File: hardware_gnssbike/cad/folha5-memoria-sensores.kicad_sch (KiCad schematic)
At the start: 18 parts, among them U501 MX25R6435F, U502 Bosch BMP585, U503 Bosch BMI270, U504 Memsic MMC5603NJ, U505 TI OPT3001DNPR

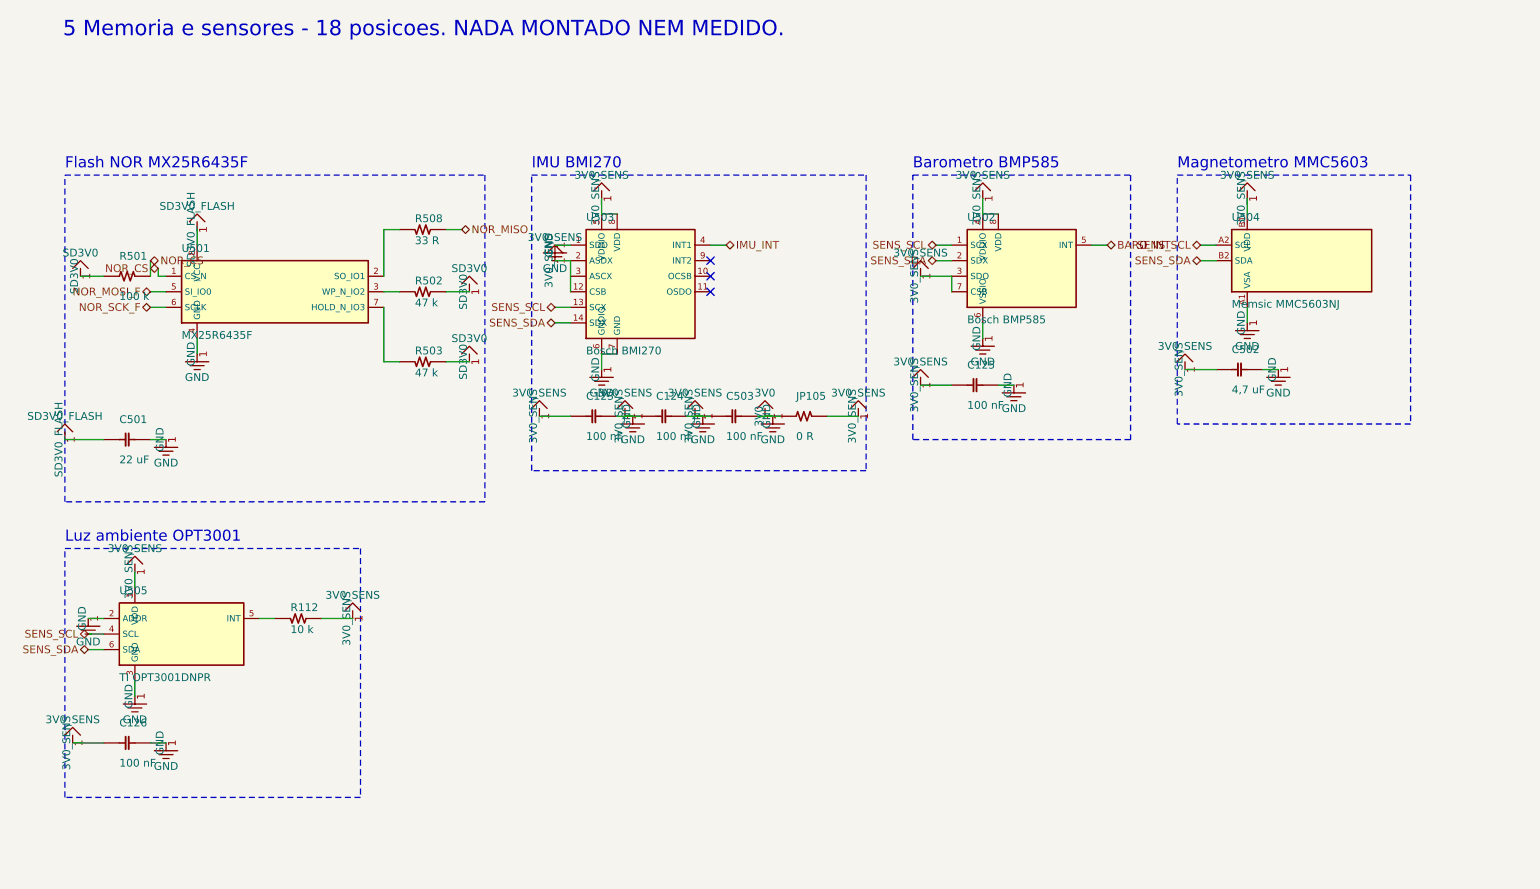
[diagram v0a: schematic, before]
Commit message: feat(hardware): spread the schematic so references, values and labels stay apart
The owner asked for the block-drawn schematic to be readable: designators
and labels were printing over each other. Power symbols now hide the pin
number and name (each printed a "1" and the rail's name twice) and point
away from their pin, lying along the line of a side pin with the name on
that line; the decoupling shelf is a row of stood-up capacitors per rail
with one wire along the tops and one symbol per row, test points standing
too; references and values sit to the right of a standing part and between
the neighbouring lines of a lying one, and block titles, part texts and
symbol names are obstacles for the router and for symbol and label
placement. Pull-ups and pull-downs of a labelled line stand past the label,
and off the corridor when the line goes on to another anchor; the labels'
room is reserved before the members are placed; the FPC connector is
mirrored to face the panel and aligned with it, its board-side wire
continuing from the label point, with the two nets of a pass-through pin
allowed to share cells; the two cells in front of every pin belong to its
net; DISP_VDD is drawn as a rail; blocks are packed by height and sheet 1
fits an A3.

The library symbol now always holds the base drawing and the instance
carries the rotation and mirror. The generator used to write the library
already flipped and the (mirror ...) token as well, applying the transform
twice, and the earlier "measurement" of (mirror x) was inverted by that.
Measured again on minimal files: (mirror y) swaps left for right, an
instance at 90 sends the left pin to the bottom, and KiCad transforms the
field justification along with the instance.

check_sch.py passes: the netlist equals nets.py pin by pin, no new ERC
error, no wire over a component. Eight nets are closed by labels where the
maze found no path inside the block, and the solar harvester and the left
of the gauge remain crowded; SCH_DEBUG=1 exp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
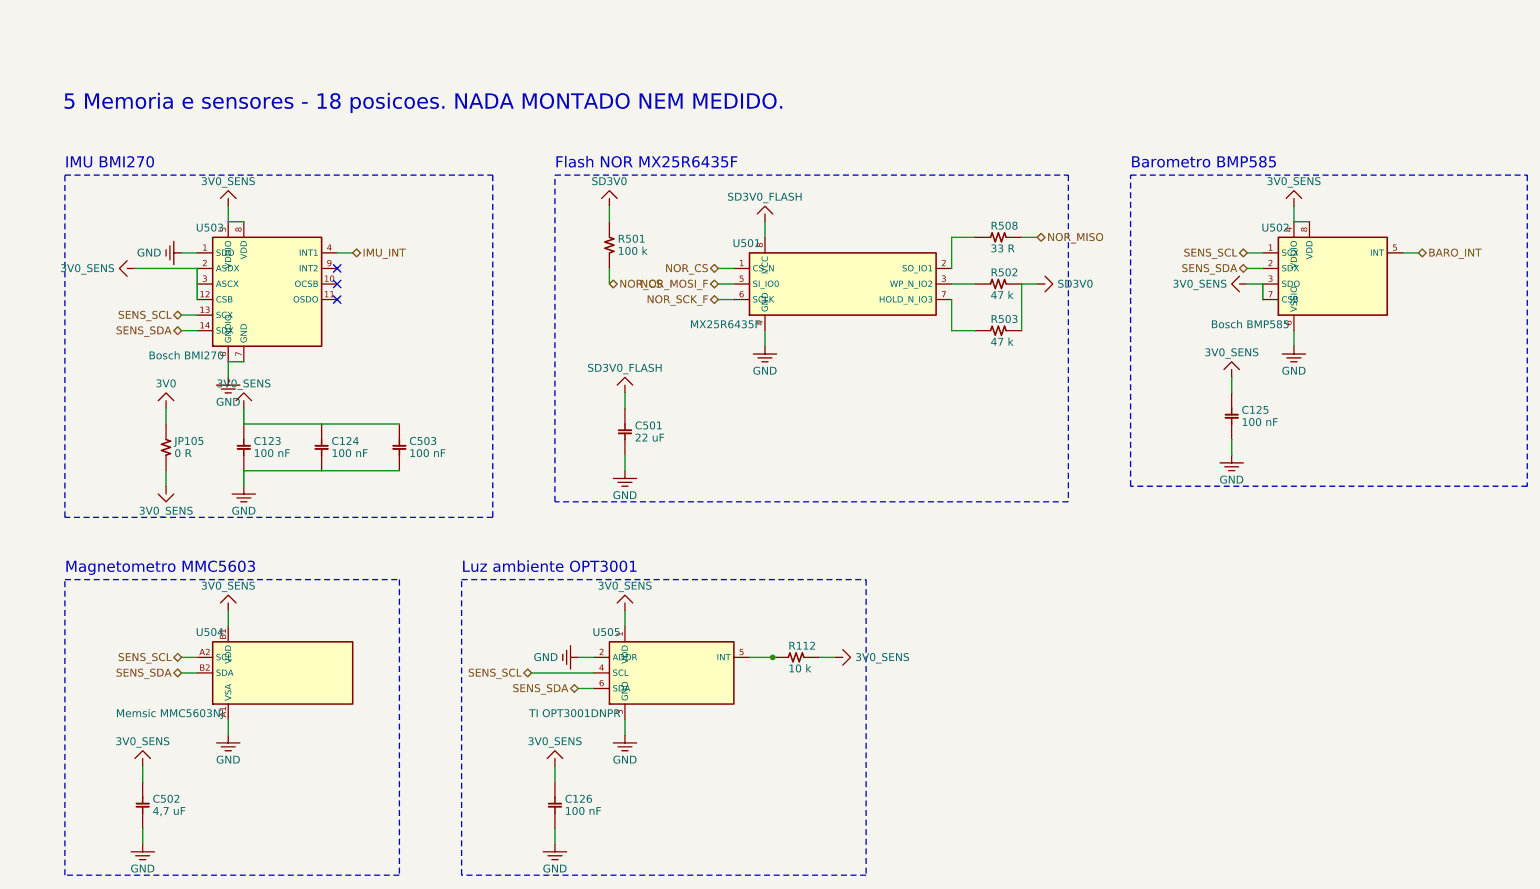
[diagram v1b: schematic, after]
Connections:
- net 3V0: no longer C123.1, C123.2, C124.1, C124.2, C125.1, C125.2, C126.1, C126.2, C501.2, C502.1, C502.2, C503.1, C503.2, JP105.2, R112.1, U501.4 (GND), U502.3 (SDO), U502.4 (VDDIO), U502.6 (VSSIO), U502.7 (CSB), U502.8 (VDD), U503.1 (SDO), U503.12 (CSB), U503.2 (ASDX), U503.3 (ASCX), U503.5 (VDDIO), U503.6 (GNDIO), U503.7 (GND), U503.8 (VDD), U504.A1 (VSA), U504.B1 (VDD), U505.1 (VDD), U505.2 (ADDR), U505.3 (GND)
- new net 3V0_SENS: C123.1, C124.1, C125.1, C126.1, C502.1, C503.1, JP105.2, R112.1, U502.3 (SDO), U502.4 (VDDIO), U502.7 (CSB), U502.8 (VDD), U503.12 (CSB), U503.2 (ASDX), U503.3 (ASCX), U503.5 (VDDIO), U503.8 (VDD), U504.B1 (VDD), U505.1 (VDD)
- new net GND: C123.2, C124.2, C125.2, C126.2, C501.2, C502.2, C503.2, U501.4 (GND), U502.6 (VSSIO), U503.1 (SDO), U503.6 (GNDIO), U503.7 (GND), U504.A1 (VSA), U505.2 (ADDR), U505.3 (GND)
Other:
- moved on the sheet: C123, C124, C125, C126, C501, C502, C503, JP105, R112, R501, R502, R503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

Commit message: feat(hardware): apply the schematic review, take either display, review the case
Apply the corrections the owner approved on 2026-10-18, in the
generators: the BMP585 land from figure 29, the RGB LED land unmirrored,
the TLV7031DCKR renumbered and fed from VBAT_SYS, the common pad of
JP301 in the middle, the OPT3001 exposed pad, the Murata land for the
buck inductors, 10 uF on PVDD and 3V3BL, a 24 V TVS on VBUS, the flash
on 3V0, pin-1 marks, the charge LEDs in the key row, the TVS next to
their connectors, the USB-C on the maker's edge line, the Same Sky
buzzer in place of the last-time-buy Murata, and an LCSC code on every
fitted part.

The board takes the JDI or the Sharp on one dual-contact Molex 503480:
JP401 picks 3V0 or 5V0, and a TPS610997 boost feeds the Sharp. A second
blind check found the connector drawn backwards (the tail enters on the
nail side); the land, the circuit order and the boost placement follow
the drawings now.

The router finds its way further: unique UUIDs per footprint, so the
DRC names the right pads; the chip antenna's own nets inside its
keep-out; JP301 turned so the two RF lines do not cross; ground vias
outside the dense chips, bent and geometrically checked ground stubs,
and a pass with the power rails first. The DRC reports no error; 60
items are still unconnected.

The case is reviewed part by part (hardware_gnssbike/12): the solar
module pockets follow the datasheet's +-0.3 mm (the case grows to 64 mm),
the keys stop 0.15 mm under the membrane, and the light sensor gets a
sealed window. The sealing of the USB-C, the floor holes and the lid
seam is left to the owner. The documents follow parts.py.

Nothing is fabricated, and the routing is still open.
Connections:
- net SD3V0 is gone; now on net 3V0: R501.1, R502.1, R503.1
- net GND: now also U505.7 (EP)
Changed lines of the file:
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@@
+	(wire
+		(pts
+			(xy 111.760 123.190) (xy 114.300 123.190)
+		)
+		(stroke (width 0) (type default))
+	)
 	(wire
 		(pts
@@
 	(wire
 		(pts
+			(xy 176.530 52.070) (xy 176.530 59.690)
+		)
+		(stroke (width 0) (type default))
+	)
+	(wire
+		(pts
+			(xy 109.220 41.910) (xy 109.220 39.370)
+		)
+		(stroke (width 0) (type default))
+	)
+	(wire
+		(pts
+			(xy 176.530 52.070) (xy 179.070 52.070)
+		)
+		(stroke (width 0) (type default))
+	)
+	(wire
+		(pts
 			(xy 36.830 74.930) (xy 36.830 72.390)
 		)
@@
 		(pts
 			(xy 111.760 107.950) (xy 111.760 105.410)
-		)
-		(stroke (width 0) (type default))
-	)
-	(wire
-		(pts
-			(xy 176.530 52.070) (xy 176.530 59.690)
-		)
-		(stroke (width 0) (type default))
-	)
-	(wire
-		(pts
-			(xy 109.220 41.910) (xy 109.220 39.370)
-		)
-		(stroke (width 0) (type default))
-	)
-	(wire
-		(pts
-			(xy 176.530 52.070) (xy 179.070 52.070)
 		)
 		(stroke (width 0) (type default))
@@
 			(effects (font (size 1.27 1.27)) (hide yes))
 		)
-		(property "Description" "flash NOR SPI; numeros 1, 2, 5 e 6 vem de 03-netlist.md"
+		(property "Description" "flash NOR SPI no 3V0; numeros 1, 2, 5 e 6 vem de 03-netlist.md. A JLCPCB tinha 2 em 2026-10-18: vai consignada (a DigiKey tinha 2.480)"
 			(at 147.32 52.07 0)
 			(effects (font (size 1.27 1.27)) (hide yes))
@@
 			(effects (font (size 1.27 1.27)) (hide yes))
 		)
-		(property "Description" "luz ambiente, 0x44 com ADDR no GND"
+		(property "Description" "luz ambiente, 0x44 com ADDR no GND; pad termico exposto (7) soldado ao GND"
 			(at 119.38 115.57000000000001 0)
 			(effects (font (size 1.27 1.27)) (hide yes))
@@
 		(pin "5")
 		(pin "6")
+		(pin "7")
 		(instances
 			(project "gnssbike"
@@
 			(effects (font (size 1.27 1.27)) (hide yes))
 		)
-		(property "Description" "pull-up do NOR_CS ao SD3V0"
+		(property "Description" "pull-up do NOR_CS ao 3V0"
 			(at 109.22 45.72 0)
 			(effects (font (size 1.27 1.27)) (hide yes))
@@
 			(effects (font (size 1.27 1.27)) (hide yes))
 		)
-		(property "Description" "pull-up do WP ao SD3V0"
+		(property "Description" "pull-up do WP ao 3V0"
 			(at 172.72 52.07 0)
 			(effects (font (size 1.27 1.27)) (hide yes))
@@
 			(effects (font (size 1.27 1.27)) (hide yes))
 		)
-		(property "Description" "pull-up do HOLD ao SD3V0"
+		(property "Description" "pull-up do HOLD ao 3V0"
 			(at 172.72 59.69 0)
 			(effects (font (size 1.27 1.27)) (hide yes))
@@
 	(symbol
 		(lib_id "power:3V0")
+		(at 109.220 39.370 0)
+		(unit 1)
+		(exclude_from_sim no)
+		(in_bom no)
+		(on_board yes)
+		(dnp no)
+		(property "Reference" "#PWR013"
+			(at 109.22 39.37 0)
+			(effects (font (size 1.27 1.27)) (hide yes))
+		)
+		(property "Value" "3V0"
+			(at 109.220 36.070 0)
+			(effects (font (size 1.27 1.27)) (justify bottom))
+		)
+		(property "Footprint" ""
+			(at 109.22 39.37 0)
+			(effects (font (size 1.27 1.27)) (hide yes))
+		)
+		(property "Datasheet" ""
+			(at 109.22 39.37 0)
+			(effects (font (size 1.27 1.27)) (hide yes))
+		)
+		(pin "1")
+		(instances
+			(project "gnssbike"
+				(path "/9c874366-f223-4aef-8b18-3e2a2bab2b25/613acabb-6b32-418f-89ed-a184dc396d24"
+					(reference "#PWR013")
+					(unit 1)
+				)
+			)
+		)
+	)
+	(symbol
+		(lib_id "power:3V0_R")
+		(at 179.070 52.070 0)
+		(unit 1)
+		(exclude_from_sim no)
+		(in_bom no)
+		(on_board yes)
+		(dnp no)
+		(property "Reference" "#PWR014"
+			(at 179.07 52.07 0)
+			(effects (font (size 1.27 1.27)) (hide yes))
+		)
+		(property "Value" "3V0"
+			(at 182.370 52.070 0)
+			(effects (font (size 1.27 1.27)) (justify left))
+		)
+		(property "Footprint" ""
+			(at 179.07 52.07 0)
+			(effects (font (size 1.27 1.27)) (hide yes))
+		)
+		(property "Datasheet" ""
+			(at 179.07 52.07 0)
+			(effects (font (size 1.27 1.27)) (hide yes))
+		)
+		(pin "1")
+		(instances
+			(project "gnssbike"
+				(path "/9c874366-f223-4aef-8b18-3e2a2bab2b25/613acabb-6b32-418f-89ed-a184dc396d24"
+					(reference "#PWR014")
+					(unit 1)
+				)
+			)
+		)
+	)
+	(symbol
+		(lib_id "power:3V0")
 		(at 36.830 72.390 0)
 		(unit 1)
@@
 		(on_board yes)
 		(dnp no)
-		(property "Reference" "#PWR013"
+		(property "Reference" "#PWR015"
 			(at 36.83 72.39 0)
 			(effects (font (size 1.27 1.27)) (hide yes))
@@
 			(project "gnssbike"
 				(path "/9c874366-f223-4aef-8b18-3e2a2bab2b25/613acabb-6b32-418f-89ed-a184dc396d24"
-					(reference "#PWR013")
+					(reference "#PWR015")
 					(unit 1)
 				)
@@
 		(on_board yes)
 		(dnp no)
-		(property "Reference" "#PWR014"
+		(property "Reference" "#PWR016"
 			(at 36.83 85.09 0)
 			(effects (font (size 1.27 1.27)) (hide yes))
@@
 			(project "gnssbike"
 				(path "/9c874366-f223-4aef-8b18-3e2a2bab2b25/613acabb-6b32-418f-89ed-a184dc396d24"
-					(reference "#PWR014")
+					(reference "#PWR016")
 					(unit 1)
 				)
@@
 		(on_board yes)
 		(dnp no)
-		(property "Reference" "#PWR015"
+		(property "Reference" "#PWR017"
 			(at 146.04999999999998 113.03 0)
 			(effects (font (size 1.27 1.27)) (hide yes))
@@
 			(project "gnssbike"
 				(path "/9c874366-f223-4aef-8b18-3e2a2bab2b25/613acabb-6b32-418f-89ed-a184dc396d24"
-					(reference "#PWR015")
+					(reference "#PWR017")
 					(unit 1)
 				)
@@
 		(on_board yes)
 		(dnp no)
-		(property "Reference" "#PWR016"
+		(property "Reference" "#PWR018"
 			(at 210.82 67.30999999999999 0)
 			(effects (font (size 1.27 1.27)) (hide yes))
@@
 			(project "gnssbike"
 				(path "/9c874366-f223-4aef-8b18-3e2a2bab2b25/613acabb-6b32-418f-89ed-a184dc396d24"
-					(reference "#PWR016")
+					(reference "#PWR018")
 					(unit 1)
 				)
@@
 		(on_board yes)
 		(dnp no)
-		(property "Reference" "#PWR017"
+		(property "Reference" "#PWR019"
 			(at 33.02 130.81 0)
 			(effects (font (size 1.27 1.27)) (hide yes))
@@
 			(project "gnssbike"
 				(path "/9c874366-f223-4aef-8b18-3e2a2bab2b25/613acabb-6b32-418f-89ed-a184dc396d24"
-					(reference "#PWR017")
+					(reference "#PWR019")
 					(unit 1)
 				)
@@
 		(on_board yes)
 		(dnp no)
-		(property "Reference" "#PWR018"
+		(property "Reference" "#PWR020"
 			(at 100.33 130.81 0)
 			(effects (font (size 1.27 1.27)) (hide yes))
@@
 			(project "gnssbike"
 				(path "/9c874366-f223-4aef-8b18-3e2a2bab2b25/613acabb-6b32-418f-89ed-a184dc396d24"
-					(reference "#PWR018")
+					(reference "#PWR020")
 					(unit 1)
 				)
@@
 		(on_board yes)
 		(dnp no)
-		(property "Reference" "#PWR019"
+		(property "Reference" "#PWR021"
 			(at 46.99 39.37 0)
 			(effects (font (size 1.27 1.27)) (hide yes))
@@
 			(project "gnssbike"
 				(path "/9c874366-f223-4aef-8b18-3e2a2bab2b25/613acabb-6b32-418f-89ed-a184dc396d24"
-					(reference "#PWR019")
+					(reference "#PWR021")
 					(unit 1)
 				)
@@
 		(on_board yes)
 		(dnp no)
-		(property "Reference" "#PWR020"
+		(property "Reference" "#PWR022"
 			(at 220.98 39.37 0)
 			(effects (font (size 1.27 1.27)) (hide yes))
@@
 			(project "gnssbike"
 				(path "/9c874366-f223-4aef-8b18-3e2a2bab2b25/613acabb-6b32-418f-89ed-a184dc396d24"
-					(reference "#PWR020")
+					(reference "#PWR022")
 					(unit 1)
 				)
@@
 		(on_board yes)
 		(dnp no)
-		(property "Reference" "#PWR021"
+		(property "Reference" "#PWR023"
 			(at 213.36 52.07 0)
 			(effects (font (size 1.27 1.27)) (hide yes))
@@
 			(project "gnssbike"
 				(path "/9c874366-f223-4aef-8b18-3e2a2bab2b25/613acabb-6b32-418f-89ed-a184dc396d24"
-					(reference "#PWR021")
+					(reference "#PWR023")
 					(unit 1)
 				)
@@
 		(on_board yes)
 		(dnp no)
-		(property "Reference" "#PWR022"
+		(property "Reference" "#PWR024"
 			(at 31.749999999999996 49.53 0)
 			(effects (font (size 1.27 1.27)) (hide yes))
@@
 			(project "gnssbike"
 				(path "/9c874366-f223-4aef-8b18-3e2a2bab2b25/613acabb-6b32-418f-89ed-a184dc396d24"
-					(reference "#PWR022")
+					(reference "#PWR024")
 					(unit 1)
 				)
@@
 		(on_board yes)
 		(dnp no)
-		(property "Reference" "#PWR023"
+		(property "Reference" "#PWR025"
 			(at 46.99 105.41 0)
 			(effects (font (size 1.27 1.27)) (hide yes))
@@
 			(project "gnssbike"
 				(path "/9c874366-f223-4aef-8b18-3e2a2bab2b25/613acabb-6b32-418f-89ed-a184dc396d24"
-					(reference "#PWR023")
+					(reference "#PWR025")
 					(unit 1)
 				)
@@
 		(on_board yes)
 		(dnp no)
-		(property "Reference" "#PWR024"
+		(property "Reference" "#PWR026"
 			(at 111.76 105.41 0)
 			(effects (font (size 1.27 1.27)) (hide yes))
@@
 			(effects (font (size 1.27 1.27)) (hide yes))
 		)
-		(pin "1")
-		(instances
-			(project "gnssbike"
-				(path "/9c874366-f223-4aef-8b18-3e2a2bab2b25/613acabb-6b32-418f-89ed-a184dc396d24"
-					(reference "#PWR024")
-					(unit 1)
-				)
-			)
-		)
-	)
-	(symbol
-		(lib_id "power:SD3V0")
-		(at 109.220 39.370 0)
-		(unit 1)
-		(exclude_from_sim no)
-		(in_bom no)
-		(on_board yes)
-		(dnp no)
-		(property "Reference" "#PWR025"
-			(at 109.22 39.37 0)
-			(effects (font (size 1.27 1.27)) (hide yes))
-		)
-		(property "Value" "SD3V0"
-			(at 109.220 36.070 0)
-			(effects (font (size 1.27 1.27)) (justify bottom))
-		)
-		(property "Footprint" ""
-			(at 109.22 39.37 0)
-			(effects (font (size 1.27 1.27)) (hide yes))
-		)
-		(property "Datasheet" ""
-			(at 109.22 39.37 0)
-			(effects (font (size 1.27 1.27)) (hide yes))
-		)
-		(pin "1")
-		(instances
-			(project "gnssbike"
-				(path "/9c874366-f223-4aef-8b18-3e2a2bab2b25/613acabb-6b32-418f-89ed-a184dc396d24"
-					(reference "#PWR025")
-					(unit 1)
-				)
-			)
-		)
-	)
-	(symbol
-		(lib_id "power:SD3V0_R")
-		(at 179.070 52.070 0)
-		(unit 1)
-		(exclude_from_sim no)
-		(in_bom no)
-		(on_board yes)
-		(dnp no)
-		(property "Reference" "#PWR026"
-			(at 179.07 52.07 0)
-			(effects (font (size 1.27 1.27)) (hide yes))
-		)
-		(property "Value" "SD3V0"
-			(at 182.370 52.070 0)
-			(effects (font (size 1.27 1.27)) (justify left))
-		)
-		(property "Footprint" ""
-			(at 179.07 52.07 0)
-			(effects (font (size 1.27 1.27)) (hide yes))
-		)
-		(property "Datasheet" ""
-			(at 179.07 52.07 0)
-			(effects (font (size 1.27 1.27)) (hide yes))
-		)
